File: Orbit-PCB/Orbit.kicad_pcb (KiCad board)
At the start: 2 copper layers, 304.8 x 145.3 mm, 285 parts, among them J1 PJ-3200B-4A, J10 Breakaway_Tabs, J11 PJ-3200B-4A, J12 AVR-ISP-6, J13 Breakaway_Tabs, J14 Breakaway_Tabs, J17 Breakaway_Tabs, J18 Breakaway_Tabs, J19 Breakaway_Tabs, J2 AVR-ISP-6, J20 Breakaway_Tabs, J3 Breakaway_Tabs, J5 Breakaway_Tabs, J6 Breakaway_Tabs, J7 Breakaway_Tabs, J9 Breakaway_Tabs, Q1 2N7002, Q2 2N7002, SW1 SW_Push, SW2 SW_Push, U1 ATmega32U4-MU, U2 PRTR5V0U2X, U3 ATmega32U4-MU, U4 PRTR5V0U2X, Y1 16MHz, Y2 16MHz

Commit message: Compact the panel slightly
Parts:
- moved D38 1.59 mm to (254.8, 38.1)
- moved D42 1.59 mm to (315.5, 53.2)
- moved D45 1.59 mm to (254.8, 57.1)
- moved D49 1.59 mm to (315.5, 64.3)
- moved D52 1.59 mm to (254.8, 76.2)
- moved D56 1.59 mm to (315.5, 80.1)
- moved D59 1.59 mm to (254.8, 95.2)
- moved D63 1.59 mm to (314.3, 96.0)
- moved D66 1.59 mm to (254.8, 114.3)
- moved D68 1.59 mm to (278.6, 121.4)
- moved J19 1.59 mm to (266.7, 31.0)
- moved MX38 1.59 mm to (266.7, 40.5)
- moved MX45 1.59 mm to (266.7, 59.5)
- moved MX52 1.59 mm to (266.7, 78.6)
- moved MX59 1.59 mm to (266.7, 97.6)
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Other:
- board size 304.8 x 145.3 mm -> 303.2 x 145.3 mm

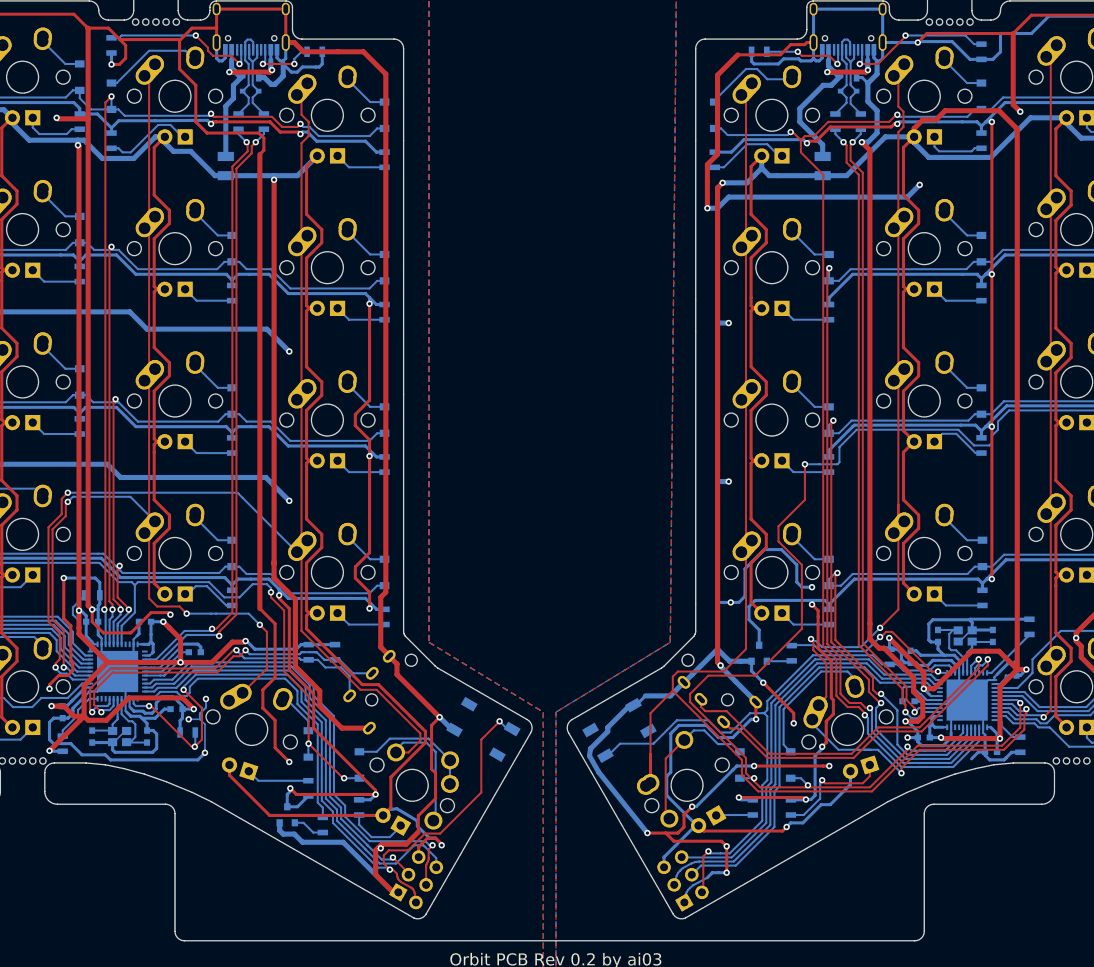
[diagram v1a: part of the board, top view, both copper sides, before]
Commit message: Simplify outline
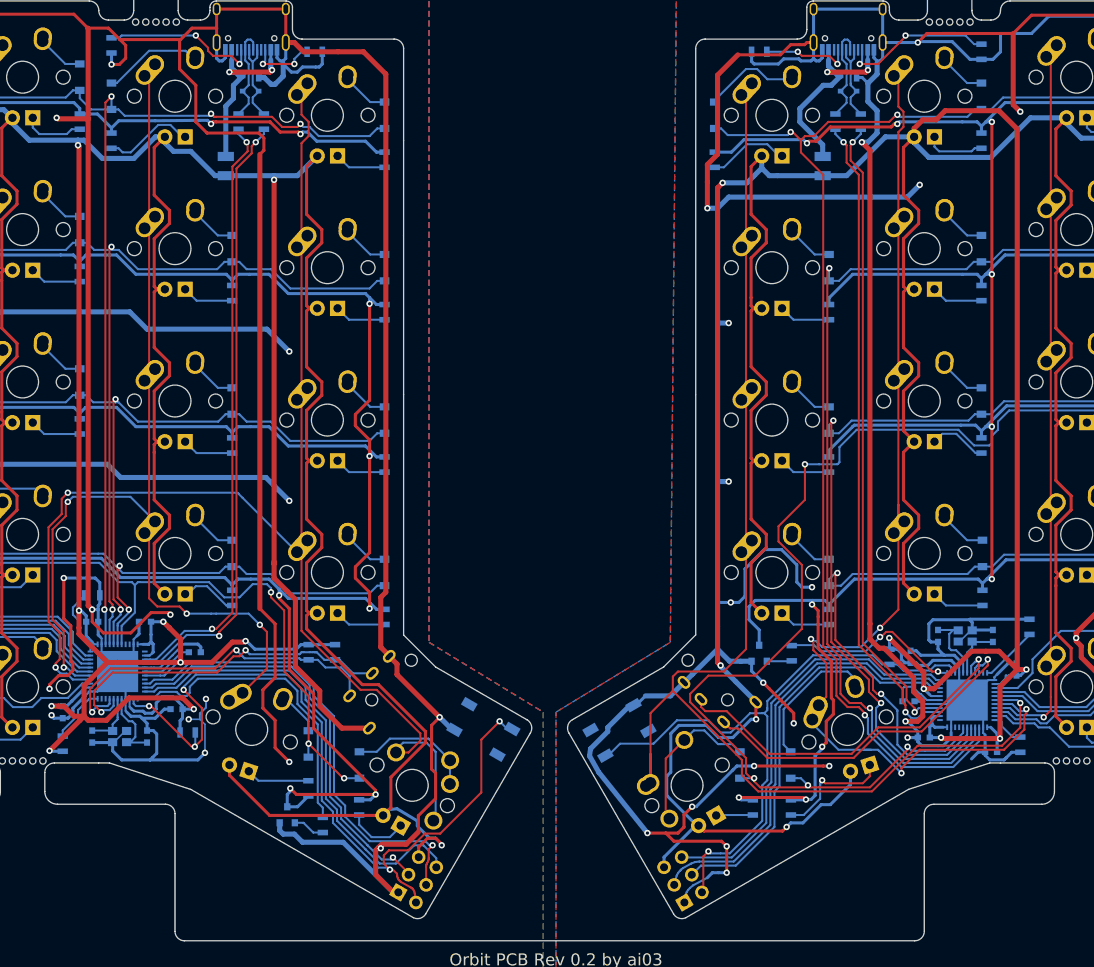
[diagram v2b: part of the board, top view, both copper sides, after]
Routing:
- net GND: track 1288.7 -> 1273.9 mm, vias 32 -> 33
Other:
- outline, holes or cut-outs redrawn

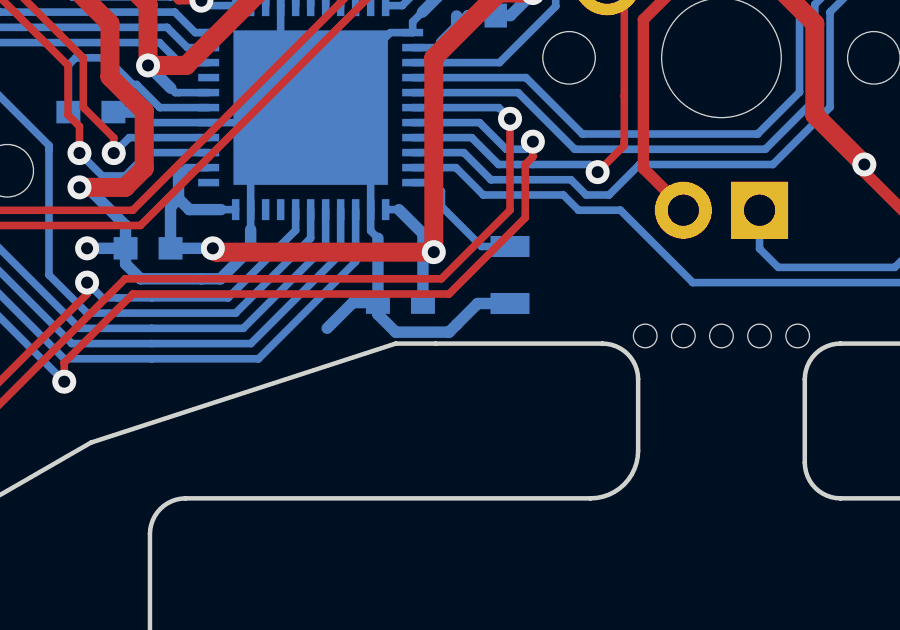
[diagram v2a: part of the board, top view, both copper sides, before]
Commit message: Fix trace too close to edge
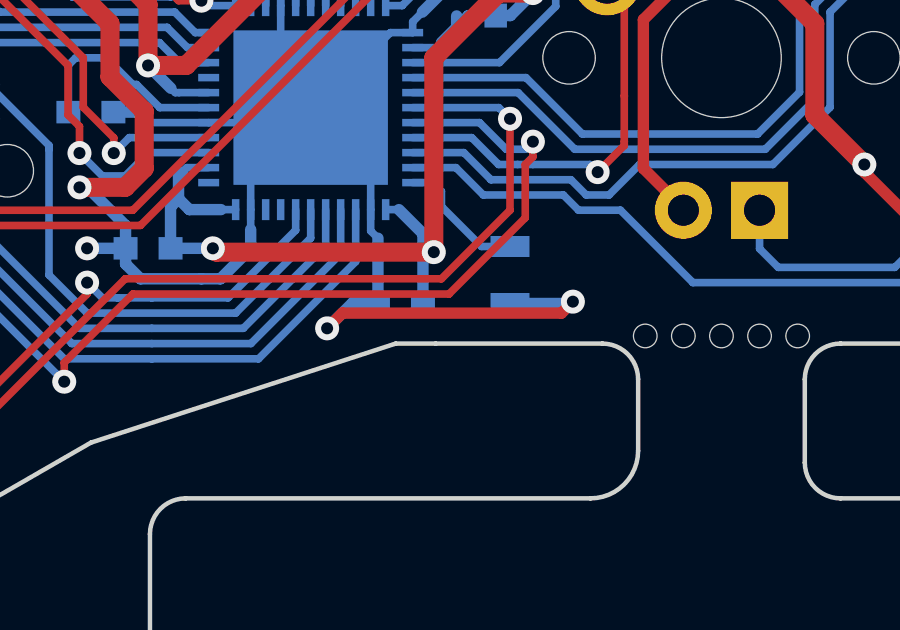
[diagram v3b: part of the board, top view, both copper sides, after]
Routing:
- net GNDA: track 1075.9 -> 1081.2 mm, vias 31 -> 33
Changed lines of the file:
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@@
     (thickness 1.6)
     (drawings 229)
-    (tracks 4040)
+    (tracks 4041)
     (zones 0)
     (modules 285)
@@
   (segment (start 236.20025 120.31275) (end 236.20025 122.45975) (width 0.381) (layer B.Cu) (net 115))
   (segment (start 235.957 120.0695) (end 236.20025 120.31275) (width 0.254) (layer B.Cu) (net 115))
-  (segment (start 238.8235 123.19) (end 238.5695 123.444) (width 0.381) (layer B.Cu) (net 115))
-  (segment (start 238.5695 123.444) (end 236.7915 123.444) (width 0.381) (layer B.Cu) (net 115))
-  (segment (start 236.20025 122.85275) (end 236.20025 122.45975) (width 0.381) (layer B.Cu) (net 115))
-  (segment (start 236.7915 123.444) (end 236.20025 122.85275) (width 0.381) (layer B.Cu) (net 115))
   (segment (start 232.957 113.5135) (end 232.957 112.55975) (width 0.254) (layer B.Cu) (net 115))
   (segment (start 237.357 113.45975) (end 236.61575 113.45975) (width 0.254) (layer B.Cu) (net 115))
@@
   (segment (start 227.7865 121.17) (end 227.7865 120.65) (width 0.381) (layer B.Cu) (net 115))
   (segment (start 228.2825 121.666) (end 227.7865 121.17) (width 0.381) (layer B.Cu) (net 115))
-  (segment (start 239.5245 122.489) (end 238.8235 123.19) (width 0.381) (layer B.Cu) (net 115))
-  (segment (start 240.6015 122.489) (end 239.5245 122.489) (width 0.381) (layer B.Cu) (net 115))
   (segment (start 192.259679 116.608853) (end 192.572647 116.608853) (width 0.381) (layer B.Cu) (net 115))
   (segment (start 237.357 113.45975) (end 237.357 113.0995) (width 0.254) (layer B.Cu) (net 115))
@@
   (segment (start 202.8825 137.541) (end 202.10781 137.541) (width 0.381) (layer B.Cu) (net 115))
   (segment (start 202.8825 137.541) (end 203.8985 137.541) (width 0.381) (layer B.Cu) (net 115))
+  (via (at 242.697 122.428) (size 0.8) (drill 0.4) (layers F.Cu B.Cu) (net 115))
+  (segment (start 240.6015 122.489) (end 242.636 122.489) (width 0.381) (layer B.Cu) (net 115))
+  (segment (start 242.636 122.489) (end 242.697 122.428) (width 0.381) (layer B.Cu) (net 115))
+  (segment (start 242.697 122.428) (end 242.316 122.809) (width 0.381) (layer F.Cu) (net 115))
+  (via (at 234.5055 123.317) (size 0.8) (drill 0.4) (layers F.Cu B.Cu) (net 115))
+  (segment (start 242.316 122.809) (end 235.0135 122.809) (width 0.381) (layer F.Cu) (net 115))
+  (segment (start 235.0135 122.809) (end 234.5055 123.317) (width 0.381) (layer F.Cu) (net 115))
   (segment (start 322.58 93.18625) (end 322.58 93.6625) (width 0.381) (layer F.Cu) (net 118))
   (segment (start 322.58 93.6625) (end 323.7865 94.869) (width 0.381) (layer F.Cu) (net 118))
@@
     (polygon
       (pts
-        (xy 219.86875 109.5375) (xy 220.6625 109.5375) (xy 220.6625 127.79375) (xy 219.86875 127.79375)
+        (xy 219.86875 109.5375) (xy 220.6625 109.5375) (xy 220.6625 130.96875) (xy 219.86875 130.96875)
+      )
+    )
+  )
+  (zone (net 0) (net_name "") (layer F.Cu) (hatch edge 0.508)
+    (connect_pads (clearance 0.381))
+    (min_thickness 0.254)
+    (keepout (tracks allowed) (vias allowed) (copperpour not_allowed))
+    (fill (arc_segments 16) (thermal_gap 0.762) (thermal_bridge_width 0.508))
+    (polygon
+      (pts
+        (xy 242.8875 111.521875) (xy 242.8875 112.315625) (xy 241.696875 112.315625) (xy 241.696875 111.521875)
       )
     )

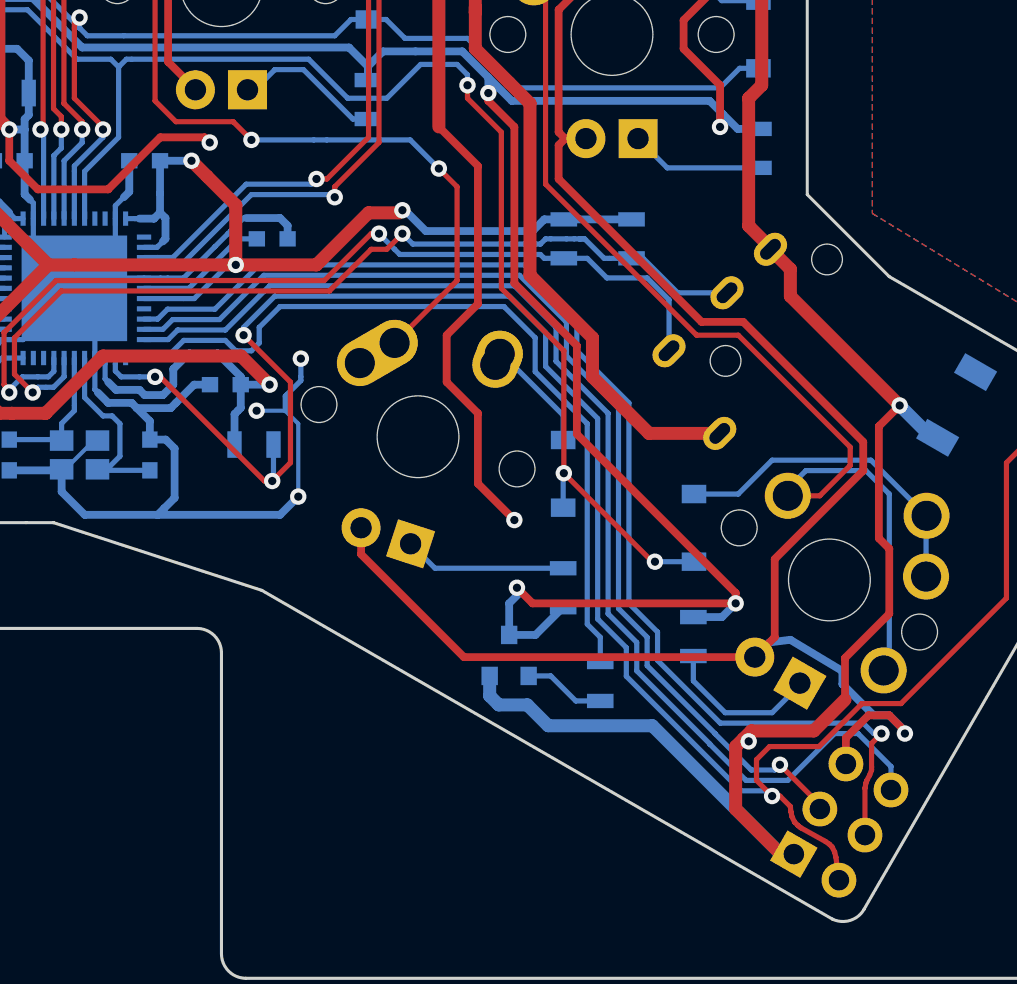
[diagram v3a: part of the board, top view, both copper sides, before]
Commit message: Move parts for easier soldering
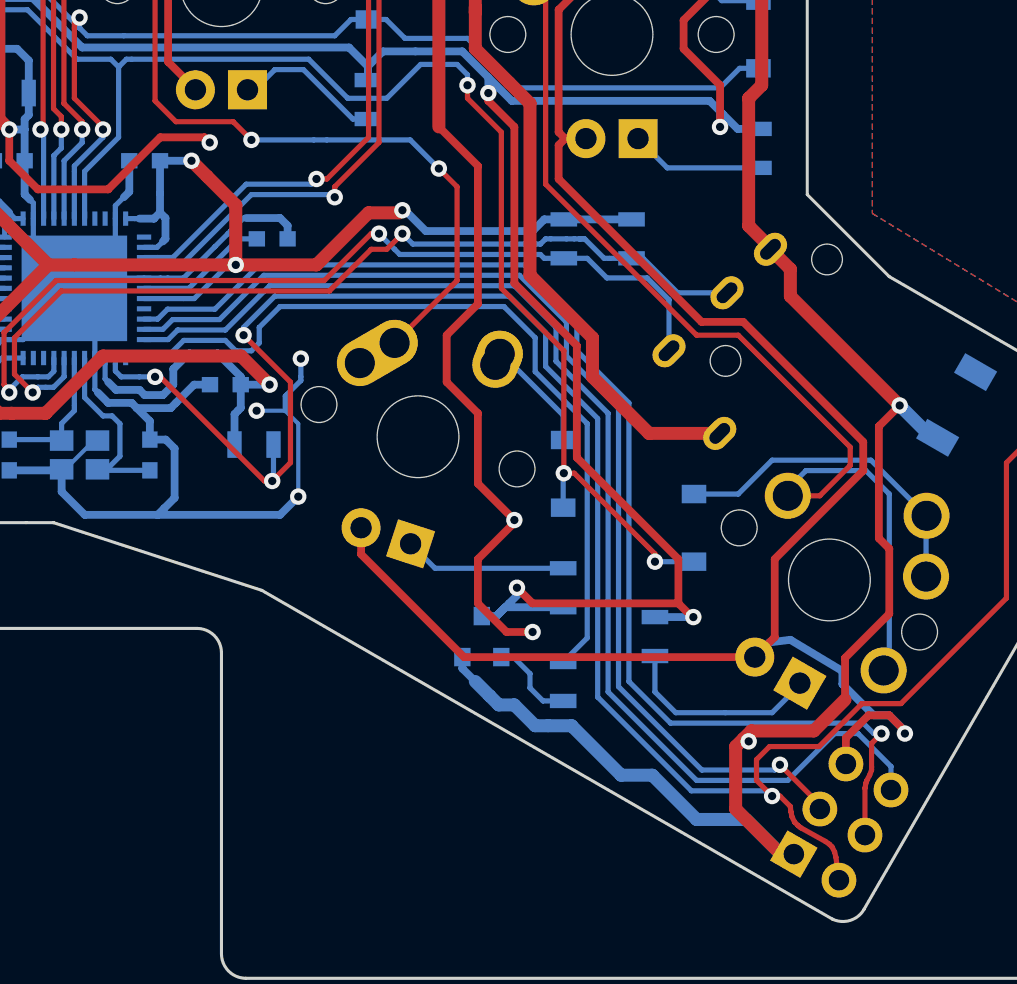
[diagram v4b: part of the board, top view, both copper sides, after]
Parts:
- added G***: LOGO, locallib:ai-4.8-mask, B.Cu at (330.2, 116.7)
- added G***: LOGO, locallib:ai-4.8-mask, B.Cu at (33.3, 116.7)
- moved R39 1.87 mm to (156.1, 129.4)
- moved R40 1.81 mm to (151.6, 131.6)
- moved Q1 1.62 mm to (147.6, 129.4)
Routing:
- net GND: track 1273.9 -> 1283.3 mm, vias 33 -> 34
- net LEDGND: track 707.2 -> 704.1 mm
- net Net-(MX34-Pad4): track 7.70 -> 9.89 mm
- net SCK: track 59.3 -> 60.7 mm
- net MOSI: track 52.7 -> 54.1 mm
- net RESET: track 100.4 -> 101.8 mm
- net MISO: track 57.8 -> 59.2 mm
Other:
- board text added: "Orbit PCB Rev. 1.0 by ai03"

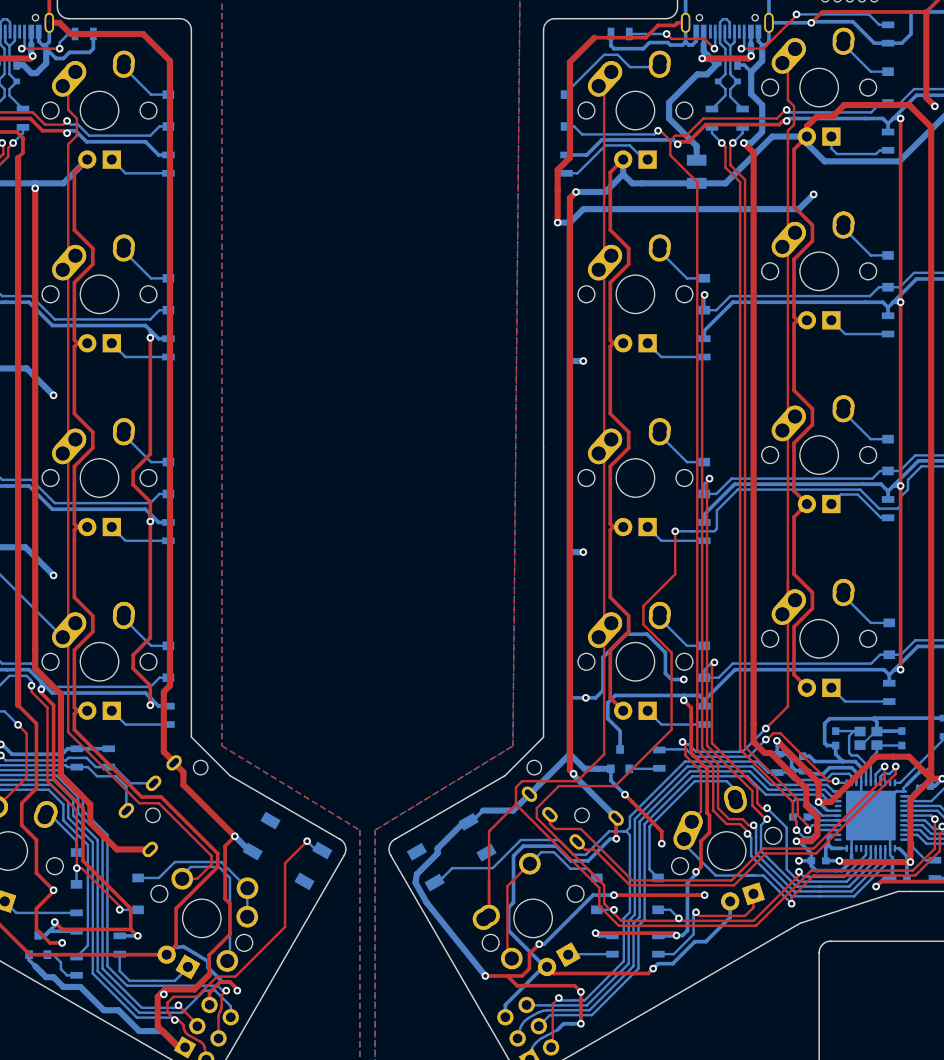
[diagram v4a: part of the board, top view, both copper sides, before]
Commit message: Move TRRS connector, too deep on most chassis
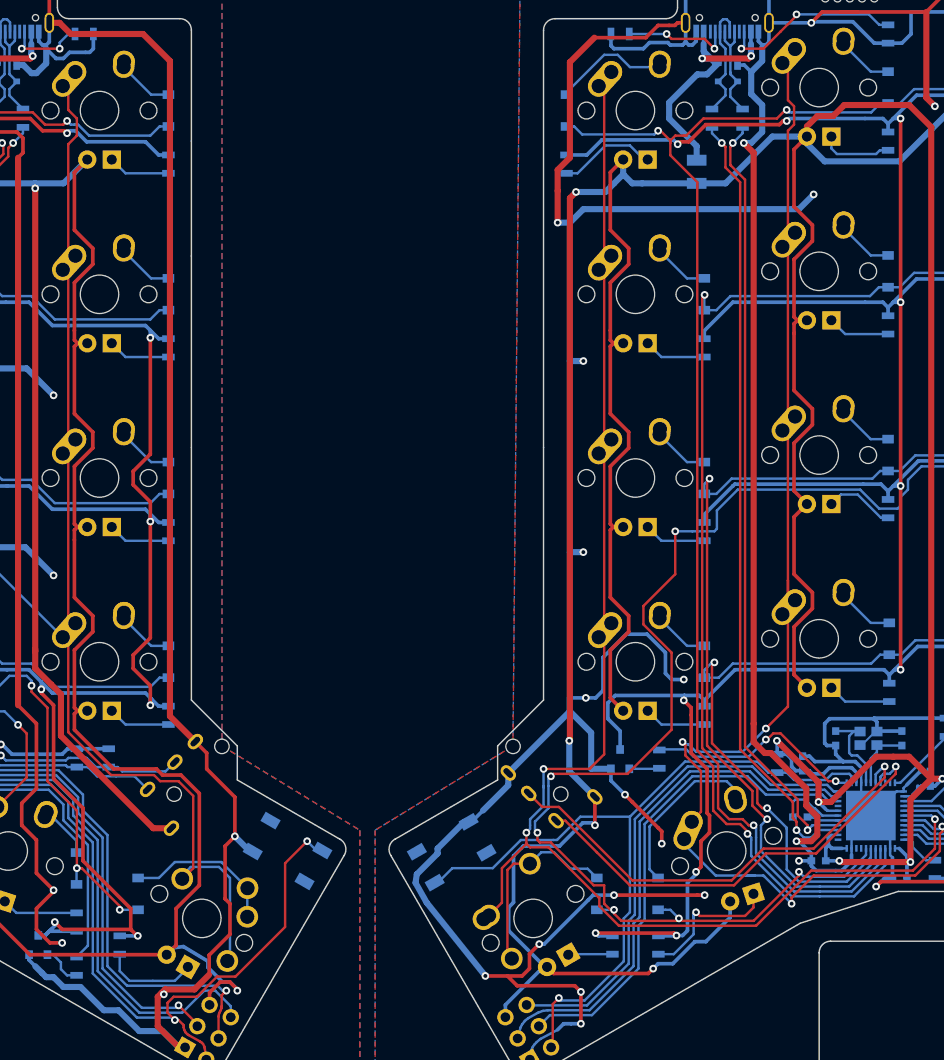
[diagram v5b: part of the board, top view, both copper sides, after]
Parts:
- moved J1 3.11 mm to (167.8, 107.7)
- moved J11 3.11 mm to (195.7, 107.7)
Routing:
- net COL0-R: track 159.8 -> 152.2 mm, vias 1 -> 3
- net +5VA: track 988.5 -> 983.3 mm
- net GNDA: track 1081.2 -> 1084.7 mm
- net SDA-R: track 43.1 -> 46.3 mm
- net SCL-R: track 45.8 -> 48.4 mm
- net ROW4-R: track 237.9 -> 240.5 mm, vias 6 -> 8
- net SCL: track 44.2 -> 46.3 mm
- net +5V: track 1029.1 -> 1027.8 mm
- net Net-(D64-Pad2): track 20.3 -> 21.3 mm
- net RESET-R: track 80.0 -> 79.5 mm
- net GND: track 1283.3 -> 1282.8 mm
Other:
- outline, holes or cut-outs redrawn
